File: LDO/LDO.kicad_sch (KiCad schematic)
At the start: 4 parts, among them U1801 L78L05_SOT89

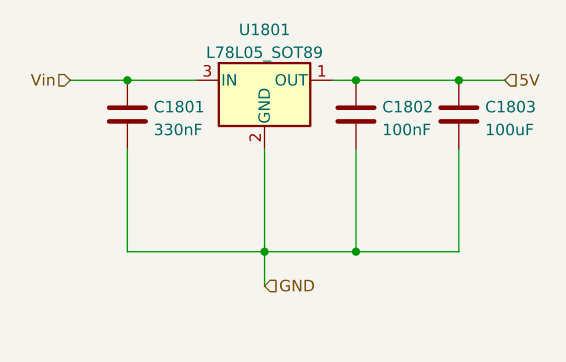
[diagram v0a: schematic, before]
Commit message: removed hierarchial labels for power symbols and replaced them with actual power symbols also updated footprint of the inductor of the 5V buck
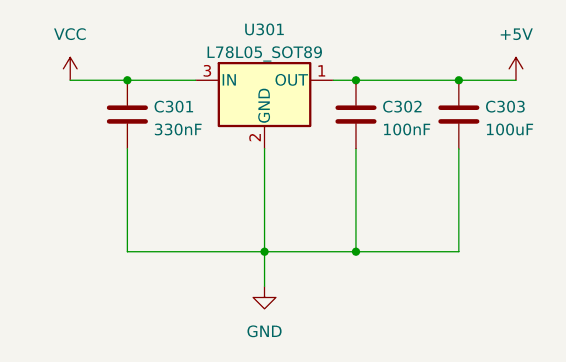
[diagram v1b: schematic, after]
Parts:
- renumbered C1801 to C301, C1802 to C302, C1803 to C303, U1801 to U301
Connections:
- net 5V renamed +5V
- net Vin renamed VCC
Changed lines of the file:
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@@
     (stroke (width 0) (type default))
   )
-  (wire (pts (xy 214.63 88.9) (xy 219.71 88.9))
+  (wire (pts (xy 214.63 88.9) (xy 220.98 88.9))
     (stroke (width 0) (type default))
   )
@@
     (stroke (width 0) (type default))
   )
-  (hierarchical_label "GND" (shape input) (at 193.04 111.76 0) (fields_autoplaced)
-    (effects (font (size 1.27 1.27)) (justify left))
-  )
-  (hierarchical_label "Vin" (shape input) (at 171.45 88.9 180) (fields_autoplaced)
-    (effects (font (size 1.27 1.27)) (justify right))
-  )
-  (hierarchical_label "5V" (shape input) (at 219.71 88.9 0) (fields_autoplaced)
-    (effects (font (size 1.27 1.27)) (justify left))
-  )
   (symbol (lib_id "Device:C") (at 203.2 92.71 0) (unit 1)
     (in_bom yes) (on_board yes) (dnp no) (fields_autoplaced)
-    (property "Reference" "C1802" (at 206.121 91.8753 0)
+    (property "Reference" "C302" (at 206.121 91.8753 0)
       (effects (font (size 1.27 1.27)) (justify left))
     )
@@
   (symbol (lib_id "Regulator_Linear:L78L05_SOT89") (at 193.04 88.9 0) (unit 1)
     (in_bom yes) (on_board yes) (dnp no) (fields_autoplaced)
-    (property "Reference" "U1801" (at 193.04 83.2952 0)
+    (property "Reference" "U301" (at 193.04 83.2952 0)
       (effects (font (size 1.27 1.27)))
     )
@@
     )
   )
+  (symbol (lib_id "power:+5V") (at 220.98 88.9 0) (unit 1)
+    (in_bom yes) (on_board yes) (dnp no) (fields_autoplaced)
+    (property "Reference" "#PWR0302" (at 220.98 92.71 0)
+      (effects (font (size 1.27 1.27)) hide)
+    )
+    (property "Value" "+5V" (at 220.98 83.82 0)
+      (effects (font (size 1.27 1.27)))
+    )
+    (property "Footprint" "" (at 220.98 88.9 0)
+      (effects (font (size 1.27 1.27)) hide)
+    )
+    (property "Datasheet" "" (at 220.98 88.9 0)
+      (effects (font (size 1.27 1.27)) hide)
+    )
+    (pin "1")
+    (instances
+      (project "LDO"
+        (path "/81bbecec-1528-4fdb-9ae5-dd524e2ba32e"
+          (reference "#PWR0302") (unit 1)
+        )
+      )
+    )
+  )
   (symbol (lib_id "Device:C") (at 177.8 92.71 0) (unit 1)
     (in_bom yes) (on_board yes) (dnp no) (fields_autoplaced)
-    (property "Reference" "C1801" (at 180.721 91.8753 0)
+    (property "Reference" "C301" (at 180.721 91.8753 0)
       (effects (font (size 1.27 1.27)) (justify left))
     )
@@
   (symbol (lib_id "Device:C") (at 214.63 92.71 0) (unit 1)
     (in_bom yes) (on_board yes) (dnp no) (fields_autoplaced)
-    (property "Reference" "C1803" (at 217.551 91.8753 0)
+    (property "Reference" "C303" (at 217.551 91.8753 0)
       (effects (font (size 1.27 1.27)) (justify left))
     )
@@
         )
       )
+    )
+  )
+  (symbol (lib_id "power:VCC") (at 171.45 88.9 0) (unit 1)
+    (in_bom yes) (on_board yes) (dnp no) (fields_autoplaced)
+    (property "Reference" "#PWR0301" (at 171.45 92.71 0)
+      (effects (font (size 1.27 1.27)) hide)
+    )
+    (property "Value" "VCC" (at 171.45 83.82 0)
+      (effects (font (size 1.27 1.27)))
+    )
+    (property "Footprint" "" (at 171.45 88.9 0)
+      (effects (font (size 1.27 1.27)) hide)
+    )
+    (property "Datasheet" "" (at 171.45 88.9 0)
+      (effects (font (size 1.27 1.27)) hide)
+    )
+    (pin "1")
+    (instances
+      (project "LDO"
+        (path "/81bbecec-1528-4fdb-9ae5-dd524e2ba32e"
+          (reference "#PWR0301") (unit 1)
+        )
+      )
+    )
+  )
+  (symbol (lib_id "power:GND") (at 193.04 111.76 0) (unit 1)
+    (in_bom yes) (on_board yes) (dnp no) (fields_autoplaced)
+    (property "Reference" "#PWR0303" (at 193.04 118.11 0)
+      (effects (font (size 1.27 1.27)) hide)
+    )
+    (property "Value" "GND" (at 193.04 116.84 0)
+      (effects (font (size 1.27 1.27)))
+    )
+    (property "Footprint" "" (at 193.04 111.76 0)
+      (effects (font (size 1.27 1.27)) hide)
+    )
+    (property "Datasheet" "" (at 193.04 111.76 0)
+      (effects (font (size 1.27 1.27)) hide)
+    )
+    (pin "1")
+    (instances
+      (project "LDO"
+        (path "/81bbecec-1528-4fdb-9ae5-dd524e2ba32e"
+          (reference "#PWR0303") (unit 1)
+        )
+      )
